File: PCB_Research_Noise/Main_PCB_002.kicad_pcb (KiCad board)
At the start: 2 copper layers, 133.3 x 96.5 mm, 484 parts, among them IC1 TPS40211QDGQRQ1, IC2 LM5164QDDATQ1, IC3 LM3481MM_NOPB, IC4 LM3488MM, IC5 LM3478MMX_NOPB, IC6 MAX998EUT+T, Q1 AON7407, Q2 AON7407, Q3 AON7407, Q4 AON7407, Q5 AON7407, U1 INA138, U10 MCP9700AT-ETT, U11 MCP9700AT-ETT, U12 MCP9700AT-ETT, U13 MCP9700AT-ETT, U14 INA138, U15 MCP9700AT-ETT, U16 MCP9700AT-ETT, U17 MCP9700AT-ETT, U18 MCP9700AT-ETT, U19 MCP9700AT-ETT, U2 Mounting_Hole_M2, U20 MCP9700AT-ETT, U21 INA138, U22 MCP9700AT-ETT, U23 MCP9700AT-ETT, U24 Mounting_Hole_M2, U25 Mounting_Hole_M2, U26 Mounting_Hole_M2, U27 Mounting_Hole_M2, U28 Mounting_Hole_M2, U3 Mounting_Hole_M2, U4 Mounting_Hole_M2, U5 Mounting_Hole_M2, U6 INA138, U7 INA138, U8 INA138, U9 MCP9700AT-ETT

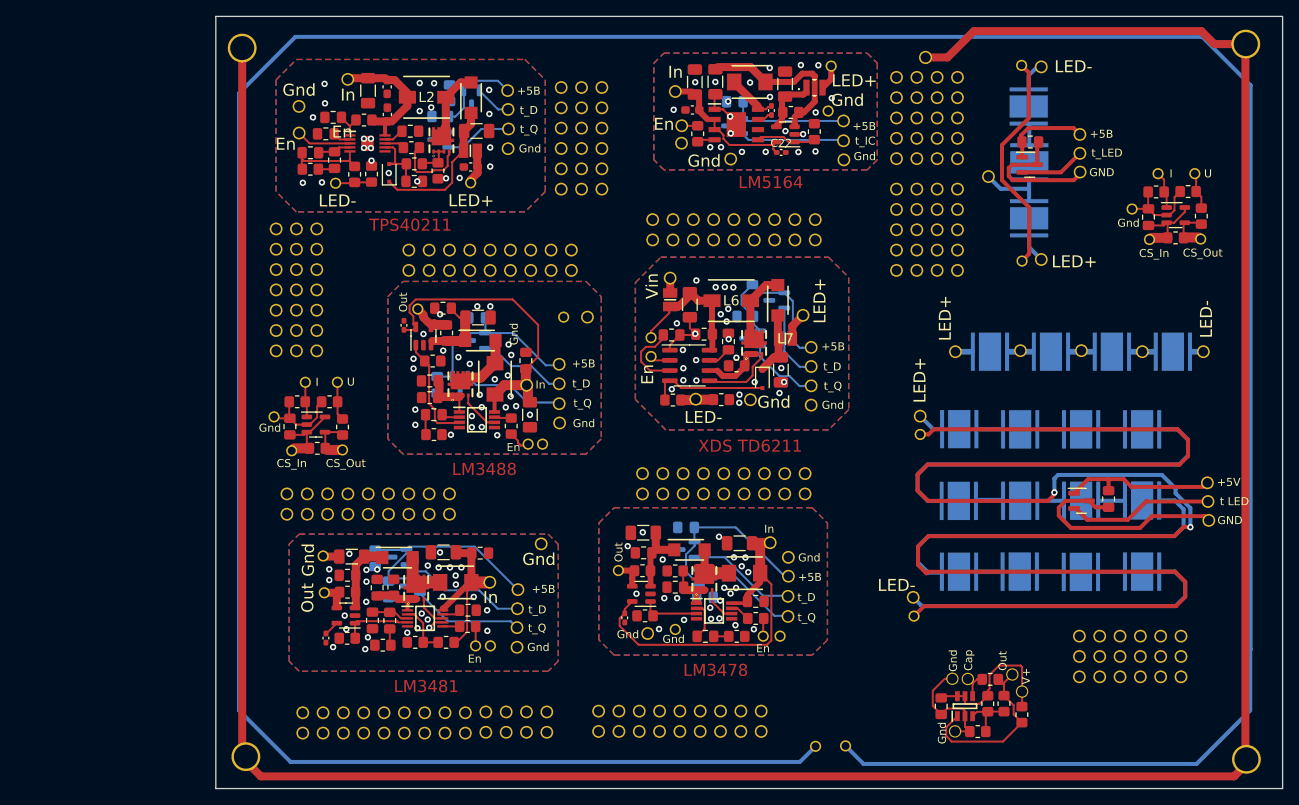
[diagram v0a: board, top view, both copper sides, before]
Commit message: Noise research for TSP40211 003
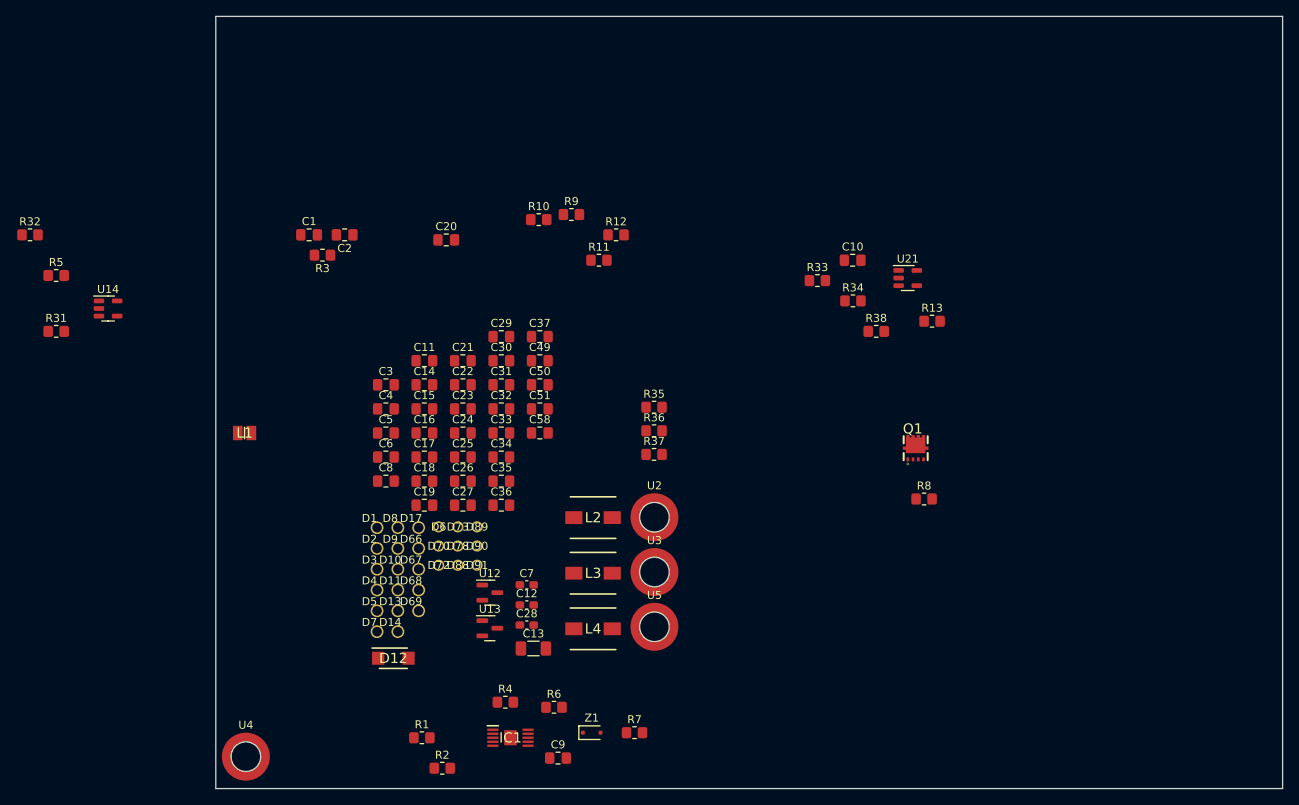
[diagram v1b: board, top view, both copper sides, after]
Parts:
- removed ? (x218): , 
- removed C38, C39, C42, C43, C46, C47, C48, C52, C53, C54, C55, C56, C57, C59, C60, C61: C, Capacitor_SMD:C_0805_2012Metric_Pad1.18x1.45mm_HandSolder
- removed C40, C41: C, Capacitor_SMD:C_1206_3216Metric_Pad1.33x1.80mm_HandSolder
- removed C44, C45: C, Capacitor_SMD:C_0402_1005Metric_Pad0.74x0.62mm_HandSolder
- removed D100, D101, D102, D103, D104, D105, D106, D107, D15, D16, D39, D53, D54: Wire_Pad_01, Flat_Wires_Pads:Wire_Hole_1mm
- removed D18, D19, D22, D23, D36, D37, D43, D44, D55, D56, D57, D98, D99: WireHole_1p5, libraries:WireHole_1p2
- removed D20: TX6211, XDS_Semi:TX6211
- removed D21, D38, D45, D46: SS36, libraries:SODFL4626X120N
- removed D24, D25, D26, D27, D28, D29, D30, D31, D32, D33 (x5), D34, D35, D47, D48, D49: LED_Cree_XHP50_6V, LED_SMD:LED_Cree-XHP50_6V
- removed D40, D52: Gnd, Flat_Wires_Pads:Wire_Hole_1mm
- removed D41, D61, D65, D77, D83, D87: Gnd, libraries:WireHole_1p2
- removed D42: In, libraries:WireHole_1p2
- removed D50: Flash LED +, libraries:WireHole_1p2
- removed D51: Out, Flat_Wires_Pads:Wire_Hole_1mm
- removed D58: Flash LED -, libraries:WireHole_1p2
- removed D59, D62, D74, D80, D84, D95: +5B, libraries:WireHole_1p2
- removed D60: t_IC, libraries:WireHole_1p2
- removed D63, D75, D81, D85: t_D, libraries:WireHole_1p2
- removed D64, D76, D82, D86: t_Q, libraries:WireHole_1p2
- removed D71: CS_Out, Flat_Wires_Pads:Wire_Hole_1mm
- removed D79: CS_In, Flat_Wires_Pads:Wire_Hole_1mm
- removed D92: +5V, libraries:WireHole_1p2
- removed D93: t LED, libraries:WireHole_1p2
- removed D94, D97: GND, libraries:WireHole_1p2
- removed D96: t_LED, libraries:WireHole_1p2
- removed IC2: LM5164QDDATQ1, libraries:SOIC127P600X170-9N
- removed IC3: LM3481MM_NOPB, libraries:SOP50P490X110-10N
- removed IC4: LM3488MM, libraries:SOP65P490X110-8N
- removed IC5: LM3478MMX_NOPB, libraries:SOP65P490X110-8N
- removed IC6: MAX998EUT+T, libraries:SOT95P280X145-6N
- removed L10, L8, L9: SRP4020TA-100M, libraries:INDPM4441X200N
- removed L5, L7: TFM201610ALC-R47MTAA, libraries:INDC2016X80N
- removed L6: TFM201610ALC-R47MTAA, libraries:INDPM5752X300N
- removed Q2, Q3, Q4, Q5: AON7407, libraries:DFN_3X3_EP
- removed R14, R15, R16, R17, R18, R19, R20, R21, R22, R23, R24, R25, R26, R27, R28, R29, R30, R39, R40, R41, R42, R43: R, Resistor_SMD:R_0805_2012Metric_Pad1.20x1.40mm_HandSolder
- removed U1, U6, U7, U8: INA138, Package_TO_SOT_SMD:SOT-23-5
- removed U10, U11, U15, U16, U17, U18, U19, U20, U22, U23, U9: MCP9700AT-ETT, Package_TO_SOT_SMD:SOT-23
- removed U24, U25, U26, U27, U28: Mounting_Hole_M2, mount_holes:Hole_screw_M1p2
- removed Z2: BZT52-C5V1J, Diode_SMD:D_SOD-323F
- C10, C5, C6: footprint Capacitor_SMD:C_0603_1608Metric_Pad1.08x0.95mm_HandSolder -> Capacitor_SMD:C_0805_2012Metric_Pad1.18x1.45mm_HandSolder
- C14, C22, C31: footprint Capacitor_SMD:C_0402_1005Metric_Pad0.74x0.62mm_HandSolder -> Capacitor_SMD:C_0805_2012Metric_Pad1.18x1.45mm_HandSolder
- C15, C16, C18, C21, C26, C29, C34, C35, C8: footprint Capacitor_SMD:C_1206_3216Metric_Pad1.33x1.80mm_HandSolder -> Capacitor_SMD:C_0805_2012Metric_Pad1.18x1.45mm_HandSolder
- C28: footprint Capacitor_SMD:C_0805_2012Metric_Pad1.18x1.45mm_HandSolder -> Capacitor_SMD:C_0603_1608Metric_Pad1.08x0.95mm_HandSolder
- C49, C50, U12, U13: moved to F.Cu
- C7: footprint Capacitor_SMD:C_1206_3216Metric_Pad1.33x1.80mm_HandSolder -> Capacitor_SMD:C_0603_1608Metric_Pad1.08x0.95mm_HandSolder
- D10, D11, D13, D14, D7, D8, D9: value Wire_Pad_01 -> WireHole_1p5; footprint Flat_Wires_Pads:Wire_Hole_1mm -> libraries:WireHole_1p2
- L3: value SRP4020TA-100M -> SRP7050AA-220M; footprint libraries:INDPM4441X200N -> libraries:INDPM5752X300N
- L4: value TFM201610ALC-R47MTAA -> SRP7050AA-220M; footprint libraries:WPN252010UR47MT -> libraries:INDPM5752X300N
- U2, U3, U4, U5: footprint mount_holes:Hole_screw_M1p2 -> Mounting_Wuerth:Mounting_Wuerth_WA-SMST-2.7mm_H1mm_9774010951
- moved R32 140.9 mm to (40.3, 80.6)
- moved R31 140.4 mm to (43.5, 92.7)
- moved U14 134.0 mm to (50.0, 89.9)
- moved D3 126.9 mm to (83.7, 122.4)
- moved D7 107.2 mm to (83.7, 130.2)
- moved D73 102.2 mm to (93.8, 117.1)
- moved D78 99.1 mm to (93.8, 119.5)
- moved D72 97.4 mm to (91.4, 121.9)
- moved D70 96.8 mm to (91.4, 119.5)
- moved U5 88.8 mm to (118.3, 129.6)
- moved D13 87.0 mm to (86.3, 127.6)
- moved D8 84.8 mm to (86.3, 117.2)
- moved R5 82.1 mm to (43.5, 85.7), turned to 0 degrees
- moved C9 80.5 mm to (106.3, 146.1)
- moved U2 79.9 mm to (118.3, 115.9)
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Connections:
- C10 pad 1: Net-(C10-Pad1) -> Net-(D11-Conn)
- C10 pad 2: Net-(C10-Pad2) -> Net-(D1-Conn)
- C11 pad 2: Net-(C10-Pad2) -> Net-(D1-Conn)
- C12 pad 1: Net-(C12-Pad1) -> Net-(D8-Conn)
- C12 pad 2: Net-(C10-Pad2) -> Net-(D1-Conn)
- C13 pad 1: Net-(C13-Pad1) -> Net-(D10-Conn)
- C13 pad 2: Net-(C10-Pad2) -> Net-(D1-Conn)
- C14 pad 1: Net-(C14-Pad1) -> Net-(D9-Conn)
- C14 pad 2: Net-(C14-Pad2) -> Net-(D1-Conn)
- C15 pad 1: Net-(C15-Pad1) -> Net-(D9-Conn)
- C15 pad 2: Net-(C15-Pad2) -> Net-(D1-Conn)
- C16 pad 1: Net-(C16-Pad1) -> Net-(D9-Conn)
- C16 pad 2: Net-(C15-Pad2) -> Net-(D1-Conn)
- C17 pad 1: Net-(C17-Pad1) -> Net-(D4-Conn)
- C17 pad 2: Net-(C17-Pad2) -> Net-(D1-Conn)
- C18 pad 1: Net-(C18-Pad1) -> Net-(D9-Conn)
- C18 pad 2: Net-(C17-Pad2) -> Net-(D1-Conn)
- C19 pad 1: Net-(C19-Pad1) -> Net-(D4-Conn)
- C19 pad 2: Net-(C17-Pad2) -> Net-(D1-Conn)
- C20 pad 1: Net-(C18-Pad1) -> Net-(D9-Conn)
- C20 pad 2: Net-(C17-Pad2) -> Net-(D1-Conn)
- C21 pad 2: Net-(C17-Pad2) -> Net-(D1-Conn)
- C22 pad 2: Net-(C15-Pad2) -> Net-(D1-Conn)
- C23 pad 1: Net-(C23-Pad1) -> Net-(C21-Pad1)
- C23 pad 2: Net-(C23-Pad2) -> Net-(D1-Conn)
- C24 pad 1: Net-(C24-Pad1) -> Net-(C22-Pad1)
- C24 pad 2: Net-(C23-Pad2) -> Net-(D1-Conn)
- C25 pad 1: Net-(C25-Pad1) -> Net-(C22-Pad1)
- C25 pad 2: Net-(C23-Pad1) -> Net-(D1-Conn)
- C26 pad 1: Net-(C26-Pad1) -> Net-(C22-Pad1)
- C26 pad 2: Net-(C23-Pad1) -> Net-(D1-Conn)
- C27 pad 1: Net-(C26-Pad1) -> Net-(C22-Pad1)
- C27 pad 2: Net-(C23-Pad1) -> Net-(D1-Conn)
- C28 pad 1: Net-(C28-Pad1) -> Net-(C22-Pad1)
- C28 pad 2: Net-(C23-Pad1) -> Net-(D1-Conn)
- C29 pad 1: Net-(C29-Pad1) -> Net-(D90-Conn)
- C29 pad 2: Net-(C23-Pad1) -> Net-(D1-Conn)
- C3 pad 1: Net-(C10-Pad2) -> Net-(D1-Conn)
- C30 pad 1: Net-(C29-Pad1) -> Net-(D10-Conn)
- C30 pad 2: Net-(C23-Pad1) -> Net-(D1-Conn)
- C31 pad 1: Net-(C31-Pad1) -> Net-(D11-Conn)
- C31 pad 2: Net-(C23-Pad1) -> Net-(D1-Conn)
- C32 pad 1: Net-(C32-Pad1) -> Net-(D11-Conn)
- C32 pad 2: Net-(C32-Pad2) -> Net-(D1-Conn)
- C33 pad 1: Net-(C33-Pad1) -> Net-(D13-Conn)
- C33 pad 2: Net-(C33-Pad2) -> Net-(D1-Conn)
- C34 pad 1: Net-(C34-Pad1) -> Net-(D13-Conn)
- C34 pad 2: Net-(C34-Pad2) -> Net-(D1-Conn)
- C35 pad 1: Net-(C35-Pad1) -> Net-(D13-Conn)
- C35 pad 2: Net-(C35-Pad2) -> Net-(D1-Conn)
- C36 pad 1: Net-(C34-Pad1) -> Net-(D11-Conn)
- C36 pad 2: Net-(C34-Pad2) -> Net-(D1-Conn)
- C37 pad 1: Net-(C35-Pad1) -> Net-(D13-Conn)
- C37 pad 2: Net-(C35-Pad2) -> Net-(D1-Conn)
- C4 pad 1: Net-(C10-Pad2) -> Net-(D1-Conn)
- C49 pad 2: Net-(C10-Pad2) -> Net-(D1-Conn)
- C5 pad 1: Net-(C12-Pad1) -> Net-(D8-Conn)
- C5 pad 2: Net-(C10-Pad2) -> Net-(D1-Conn)
- C50 pad 2: Net-(C10-Pad2) -> Net-(D1-Conn)
- C51 pad 2: Net-(C51-Pad2) -> Net-(D1-Conn)
- C58 pad 1: Net-(C58-Pad1) -> Net-(D14-Conn)
- C58 pad 2: Net-(C58-Pad2) -> Net-(D1-Conn)
- C6 pad 1: Net-(C22-Pad1) -> Net-(D73-Conn)
- C6 pad 2: Net-(C15-Pad2) -> Net-(D1-Conn)
- C7 pad 1: Net-(C22-Pad1) -> Net-(D9-Conn)
- C7 pad 2: Net-(C15-Pad2) -> Net-(D1-Conn)
- C8 pad 1: Net-(C12-Pad1) -> Net-(D8-Conn)
- C8 pad 2: Net-(C10-Pad2) -> Net-(D1-Conn)
- C9 pad 2: Net-(C10-Pad2) -> Net-(D1-Conn)
- D1 pad 1: Net-(C10-Pad2) -> Net-(D1-Conn)
- D10 pad 1: Net-(D10-Pad1) -> Net-(D10-Conn)
- D11 pad 1: Net-(C10-Pad1) -> Net-(D11-Conn)
- D12 pad 1: Net-(C13-Pad1) -> Net-(Z1-K)
- D13 pad 1: Net-(D13-Pad1) -> Net-(D13-Conn)
- D14 pad 1: Net-(D14-Pad1) -> Net-(D14-Conn)
- D2 pad 1: Net-(C15-Pad2) -> unconnected-(D2-Conn-Pad1)
- D3 pad 1: GND -> Net-(D3-Conn)
- D4 pad 1: Net-(C12-Pad1) -> Net-(D4-Conn)
- D5 pad 1: Net-(C22-Pad1) -> unconnected-(D5-Conn-Pad1)
- D69 pad 1: Net-(C10-Pad2) -> Net-(D1-Conn)
- D7 pad 1: Net-(D7-Pad1) -> Net-(D7-Conn)
- D72 pad 1: Net-(C51-Pad2) -> Net-(D1-Conn)
- D73 pad 1: Net-(D73-Pad1) -> Net-(D73-Conn)
- D8 pad 1: Net-(D7-Pad1) -> Net-(D8-Conn)
- D89 pad 1: Net-(C58-Pad2) -> Net-(D1-Conn)
- D9 pad 1: Net-(D10-Pad1) -> Net-(D9-Conn)
- D90 pad 1: Net-(D90-Pad1) -> Net-(D90-Conn)
- IC1 pad 10: Net-(C12-Pad1) -> Net-(D8-Conn)
- IC1 pad 11: Net-(C10-Pad2) -> Net-(D1-Conn)
- IC1 pad 6: Net-(C10-Pad2) -> Net-(D1-Conn)
- L1 pad 1: Net-(C10-Pad1) -> Net-(D11-Conn)
- L1 pad 2: Net-(C13-Pad1) -> Net-(D13-Conn)
- L2 pad 1: Net-(C12-Pad1) -> Net-(L2-Pad1)
- L3 pad 1: Net-(C14-Pad1) -> Net-(D4-Conn)
- L3 pad 2: Net-(C15-Pad1) -> Net-(C21-Pad1)
- L4 pad 1: Net-(C16-Pad1) -> Net-(D9-Conn)
- L4 pad 2: Net-(D13-Pad1) -> Net-(C22-Pad1)
- R1 pad 1: Net-(C10-Pad2) -> Net-(D1-Conn)
- R10 pad 1: Net-(C15-Pad2) -> Net-(C22-Pad1)
- R10 pad 2: Net-(IC2-Pad5) -> Net-(D3-Conn)
- R11 pad 1: Net-(D20-Pad6) -> Net-(D8-Conn)
- R11 pad 2: Net-(C17-Pad2) -> Net-(L2-Pad1)
- R12 pad 1: Net-(D20-Pad4) -> Net-(D10-Conn)
- R12 pad 2: Net-(D22-Pad1) -> Net-(Z1-K)
- R13 pad 1: Net-(D22-Pad1) -> Net-(D90-Conn)
- R13 pad 2: Net-(C17-Pad2) -> Net-(R13-Pad2)
- R31 pad 2: Net-(D71-Pad1) -> Net-(D9-Conn)
- R32 pad 1: Net-(C51-Pad2) -> Net-(D1-Conn)
- R33 pad 1: Net-(D73-Pad1) -> Net-(R33-Pad1)
- R33 pad 2: Net-(D71-Pad1) -> Net-(D9-Conn)
- R34 pad 1: Net-(C51-Pad2) -> Net-(D1-Conn)
- R34 pad 2: Net-(D73-Pad1) -> Net-(R33-Pad1)
- R35 pad 1: Net-(C58-Pad1) -> Net-(D14-Conn)
- R36 pad 1: Net-(C58-Pad2) -> Net-(D1-Conn)
- R37 pad 1: Net-(D90-Pad1) -> Net-(R13-Pad2)
- R38 pad 1: Net-(C58-Pad2) -> Net-(D1-Conn)
- R38 pad 2: Net-(D90-Pad1) -> Net-(R13-Pad2)
- R4 pad 2: Net-(C12-Pad1) -> Net-(D8-Conn)
- R5 pad 1: Net-(IC2-Pad4) -> Net-(D73-Conn)
- R5 pad 2: Net-(R5-Pad2) -> Net-(R33-Pad1)
- R8 pad 2: Net-(C10-Pad2) -> Net-(D1-Conn)
- R9 pad 1: Net-(C15-Pad1) -> Net-(C21-Pad1)
- R9 pad 2: Net-(C16-Pad1) -> Net-(D7-Conn)
- U12 pad 3: Net-(C10-Pad2) -> Net-(D1-Conn)
- U13 pad 3: Net-(C10-Pad2) -> Net-(D1-Conn)
- U14 pad 2: Net-(C51-Pad2) -> Net-(D1-Conn)
- U14 pad 4: Net-(D71-Pad1) -> Net-(D9-Conn)
- U21 pad 2: Net-(C58-Pad2) -> Net-(D1-Conn)
- U21 pad 3: Net-(C58-Pad1) -> Net-(D14-Conn)
- U21 pad 5: Net-(C58-Pad1) -> Net-(D14-Conn)
- Z1 pad 1: Net-(C13-Pad1) -> Net-(Z1-K)
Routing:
- net Net-(D10-Pad1): track 417.0 -> 0.00 mm
- net GND: track 346.6 -> 0.00 mm
- net Net-(D14-Pad1): track 222.8 -> 0.00 mm, vias 2 -> 0
- net Net-(D31-Pad1): track 46.5 -> 0.00 mm
- net Net-(D27-Pad1): track 45.4 -> 0.00 mm
- net Net-(C34-Pad1): track 44.9 -> 0.00 mm
- net Net-(D24-Pad2): track 40.6 -> 0.00 mm
- net Net-(C35-Pad1): track 39.5 -> 0.00 mm
- net Net-(C47-Pad1): track 29.2 -> 0.00 mm
- net Net-(C59-Pad2): track 28.1 -> 0.00 mm
- net Net-(D7-Pad1): track 28.0 -> 0.00 mm
- net Net-(C54-Pad1): track 23.7 -> 0.00 mm
- net Net-(C55-Pad1): track 23.5 -> 0.00 mm
- net Net-(C15-Pad1): track 21.5 -> 0.00 mm
- net Net-(IC6-Pad1): track 21.5 -> 0.00 mm
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- removed copper zone on B.Cu, net Net-(C10-Pad2)
- removed copper zone on F.Cu, net Net-(C10-Pad2)
- removed copper zone on B.Cu, net Net-(C15-Pad2)
- removed copper zone on F.Cu, net Net-(C15-Pad2)
- removed copper zone on B.Cu, net Net-(C17-Pad2)
- removed copper zone on F.Cu, net Net-(C17-Pad2)
- removed copper zone on B.Cu, net Net-(C23-Pad1)
- removed copper zone on F.Cu, net Net-(C23-Pad1)
- removed copper zone on B.Cu, net Net-(C34-Pad2)
- removed copper zone on F.Cu, net Net-(C34-Pad2)
- removed copper zone on B.Cu, net Net-(C35-Pad2)
- removed copper zone on F.Cu, net Net-(C35-Pad2)
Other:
- board text removed: "+"
- board text removed: "-"
- board text removed: "Cap"
- board text removed: "En"
- board text removed: "Gnd"
- board text removed: "In"
- board text removed: "LED+"
- board text removed: "LED-"
- board text removed: "LM3478"
- board text removed: "LM3481"
- board text removed: "LM3488"
- board text removed: "LM5164"
- board text removed: "Out"
- board text removed: "TPS40211"
- board text removed: "V+"
- board text removed: "Vin"
- board text removed: "XDS TD6211"
